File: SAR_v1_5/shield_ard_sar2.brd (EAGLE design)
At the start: 53.5 x 68.5 mm, 18 parts

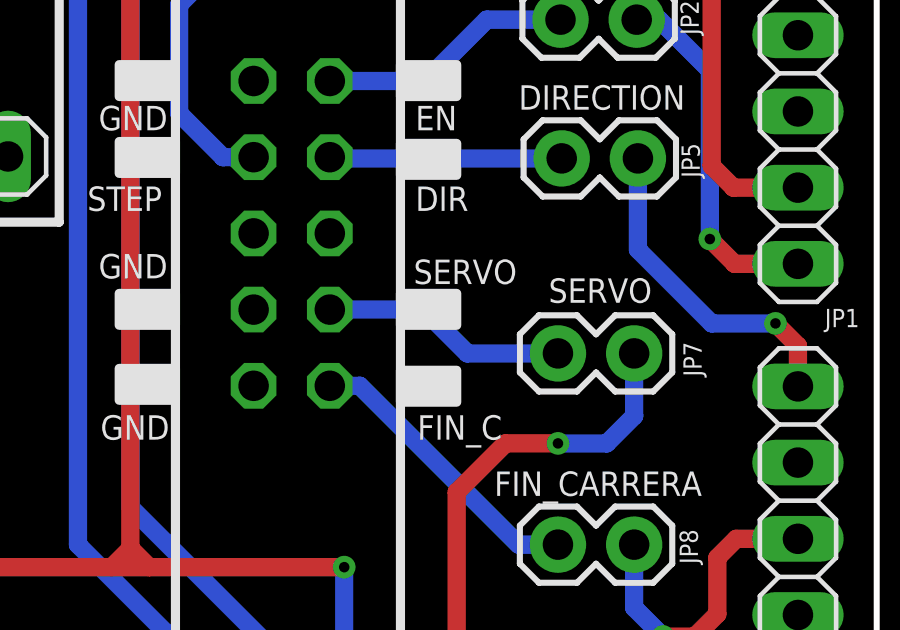
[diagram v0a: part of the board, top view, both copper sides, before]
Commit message: a filter circuit was added to servomotor control circuit in order to avoid noise in control pin
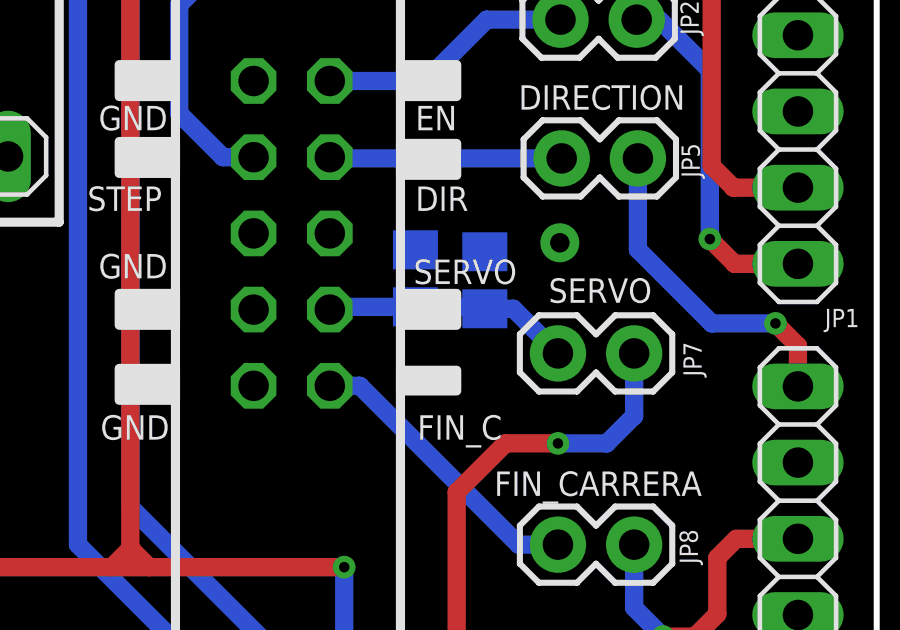
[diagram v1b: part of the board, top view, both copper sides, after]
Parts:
- added C1: 10nF, eagle-ltspice:C0805
- added R3: 1k, rcl:R0805
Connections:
- net GND: now also C1.2, R3.1
- net SERVO*: now also C1.1, R3.2
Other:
- board text removed: "SAR v1.5"
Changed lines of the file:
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@@
 <?xml version="1.0" encoding="utf-8"?>
 <!DOCTYPE eagle SYSTEM "eagle.dtd">
-<eagle version="9.5.2">
+<eagle version="9.3.0">
 <drawing>
 <settings>
@@
 <layer number="24" name="bOrigins" color="15" fill="1" visible="yes" active="yes"/>
 <layer number="25" name="tNames" color="7" fill="1" visible="yes" active="yes"/>
-<layer number="26" name="bNames" color="7" fill="1" visible="no" active="yes"/>
+<layer number="26" name="bNames" color="7" fill="1" visible="yes" active="yes"/>
 <layer number="27" name="tValues" color="7" fill="1" visible="no" active="yes"/>
-<layer number="28" name="bValues" color="7" fill="1" visible="no" active="yes"/>
+<layer number="28" name="bValues" color="7" fill="1" visible="yes" active="yes"/>
 <layer number="29" name="tStop" color="7" fill="3" visible="no" active="yes"/>
 <layer number="30" name="bStop" color="7" fill="6" visible="no" active="yes"/>
@@
 <board>
 <plain>
-<text x="-130.63128125" y="18.566940625" size="1.778" layer="22" rot="MR315">SAR v1.5</text>
 <wire x1="-0.25" y1="2.5" x2="2.5" y2="2.5" width="0.2" layer="20"/>
 <wire x1="2.5" y1="2.5" x2="5" y2="0" width="0.2" layer="20"/>
@@
 <vertex x="37.375" y="23.3125"/>
 <vertex x="39.25" y="23.3125"/>
-<vertex x="39.25" y="22.25"/>
-<vertex x="37.375" y="22.25"/>
+<vertex x="39.25" y="22.625"/>
+<vertex x="37.375" y="22.625"/>
 </polygon>
 <polygon width="0.3048" layer="21">
@@
 </element>
 <element name="MOTOR_PASO" library="pinhead" library_urn="urn:adsk.eagle:library:325" package="2X05" package3d_urn="urn:adsk.eagle:package:22470/2" value="" x="33.75" y="27.875" smashed="yes" rot="MR270">
-<attribute name="NAME" x="30.575" y="34.225" size="1.27" layer="26" ratio="10" rot="MR270"/>
+<attribute name="NAME" x="30.5875" y="31.2" size="0.8128" layer="22" font="vector" ratio="20" rot="MR270"/>
 <attribute name="POPULARITY" value="35" x="33.75" y="27.875" size="1.778" layer="28" rot="MR270" display="off"/>
 <attribute name="VALUE" x="38.195" y="34.225" size="1.27" layer="28" rot="MR270"/>
@@
 <attribute name="POPULARITY" value="10" x="7.25" y="57.5" size="1.778" layer="27" rot="R270" display="off"/>
 <attribute name="VALUE" x="3.44" y="47.975" size="1.27" layer="27"/>
+</element>
+<element name="R3" library="rcl" library_urn="urn:adsk.eagle:library:334" package="R0805" package3d_urn="urn:adsk.eagle:package:23553/2" value="1k" x="40.1875" y="26.3125" smashed="yes" rot="MR270">
+<attribute name="NAME" x="39.9175" y="23.0725" size="0.6096" layer="26" font="vector" ratio="20" rot="MR90"/>
+<attribute name="POPULARITY" value="86" x="40.1875" y="26.3125" size="1.778" layer="28" rot="MR270" display="off"/>
+<attribute name="SPICEPREFIX" value="R" x="40.1875" y="26.3125" size="1.778" layer="28" rot="MR270" display="off"/>
+<attribute name="VALUE" x="39.915" y="28.4475" size="0.6096" layer="26" font="vector" ratio="20" rot="MR90"/>
+</element>
+<element name="C1" library="eagle-ltspice" library_urn="urn:adsk.eagle:library:217" package="C0805" package3d_urn="urn:adsk.eagle:package:13265/1" value="10nF" x="37.875" y="26.375" smashed="yes" rot="MR90">
+<attribute name="NAME" x="37.8325" y="23.2925" size="0.6096" layer="26" font="vector" ratio="20" rot="MR90"/>
+<attribute name="SPICEMODEL" value="NONE" x="37.875" y="26.375" size="1.778" layer="28" rot="MR90" display="off"/>
+<attribute name="SPICEPREFIX" value="C" x="37.875" y="26.375" size="1.778" layer="28" rot="MR90" display="off"/>
+<attribute name="VALUE" x="37.6475" y="28.48" size="0.6096" layer="26" font="vector" ratio="20" rot="MR90"/>
 </element>
 </elements>
@@
 <via x="9.3125" y="5.6875" extent="1-16" drill="0.65" diameter="1.3"/>
 <via x="19.1875" y="35.625" extent="1-16" drill="0.65" diameter="1.3"/>
+<contactref element="C1" pad="2"/>
+<contactref element="R3" pad="1"/>
+<via x="42.6875" y="27.5625" extent="1-16" drill="0.65" diameter="1.3"/>
 </signal>
 <signal name="HV_5V">
@@
 <contactref element="JP7" pad="1"/>
 <contactref element="MOTOR_PASO" pad="7"/>
-<wire x1="39.605" y1="23.875" x2="38.145" y2="25.335" width="0.6096" layer="16"/>
-<wire x1="35.02" y1="25.335" x2="38.145" y2="25.335" width="0.6096" layer="16"/>
-<wire x1="39.605" y1="23.875" x2="42.625" y2="23.875" width="0.6096" layer="16"/>
+<contactref element="R3" pad="2"/>
+<contactref element="C1" pad="1"/>
+<wire x1="42.625" y1="23.875" x2="41.1375" y2="25.3625" width="0.6096" layer="16"/>
+<wire x1="41.1375" y1="25.3625" x2="40.1875" y2="25.3625" width="0.6096" layer="16"/>
+<wire x1="40.1875" y1="25.3625" x2="40.125" y2="25.425" width="0.6096" layer="16"/>
+<wire x1="40.125" y1="25.425" x2="37.875" y2="25.425" width="0.6096" layer="16"/>
+<wire x1="37.875" y1="25.425" x2="35.11" y2="25.425" width="0.6096" layer="16"/>
+<wire x1="35.11" y1="25.425" x2="35.02" y2="25.335" width="0.6096" layer="16"/>
 </signal>
 <signal name="N$41">
